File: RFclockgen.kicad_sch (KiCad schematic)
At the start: 10 parts, among them J1 Conn_01x04_Pin, J3 Conn_01x02_Pin, U2 ESP32-S3-WROOM-1, U3 AP2112K-3.3

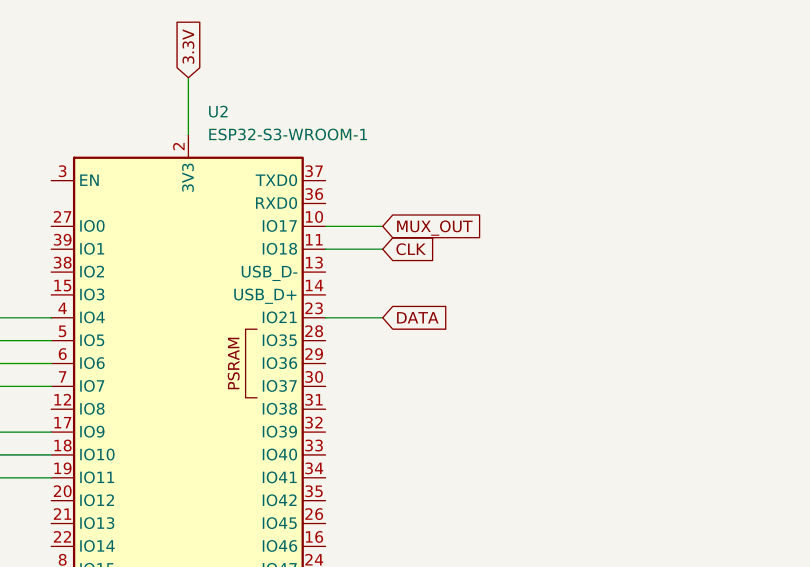
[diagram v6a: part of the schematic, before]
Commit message: Fix: fixed usb receptacle
Changed footprint and wired up usb C
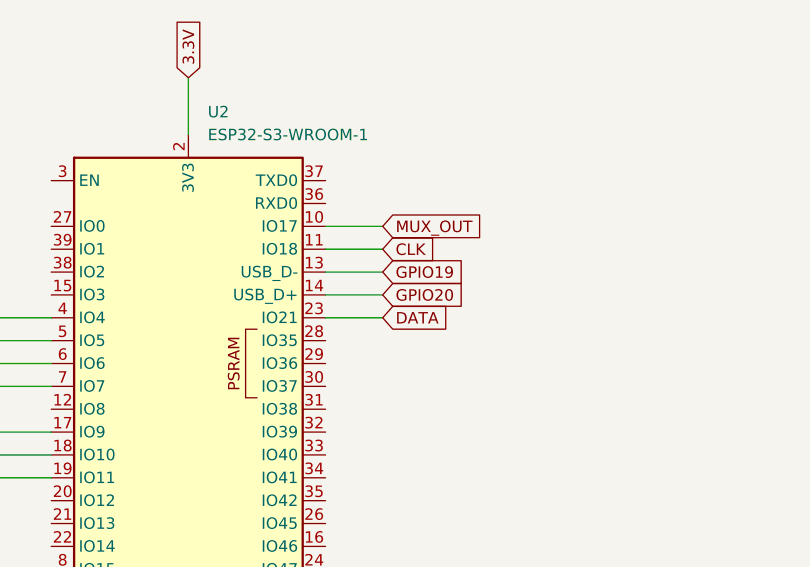
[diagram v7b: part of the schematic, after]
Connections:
- net GPIO19: now reaches U2.13 (USB_D-)
- net GPIO20: now reaches U2.14 (USB_D+)
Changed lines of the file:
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@@
+	(wire
+		(pts
+			(xy 172.72 68.58) (xy 179.07 68.58)
+		)
+		(stroke
+			(width 0)
+			(type default)
+		)
+	)
 	(wire
 		(pts
@@
 	(wire
 		(pts
+			(xy 172.72 66.04) (xy 179.07 66.04)
+		)
+		(stroke
+			(width 0)
+			(type default)
+		)
+	)
+	(wire
+		(pts
 			(xy 118.11 83.82) (xy 142.24 83.82)
 		)
@@
 		)
 	)
+	(global_label "GPIO19"
+		(shape input)
+		(at 179.07 66.04 0)
+		(fields_autoplaced yes)
+		(effects
+			(font
+				(size 1.27 1.27)
+			)
+			(justify left)
+		)
+		(property "Intersheetrefs" "${INTERSHEET_REFS}"
+			(at 188.9495 66.04 0)
+			(effects
+				(font
+					(size 1.27 1.27)
+				)
+				(justify left)
+				(hide yes)
+			)
+		)
+	)
 	(global_label "3.3V"
 		(shape input)
@@
 			(effects
 				(font
+					(size 1.27 1.27)
+				)
+				(justify left)
+				(hide yes)
+			)
+		)
+	)
+	(global_label "GPIO20"
+		(shape input)
+		(at 179.07 68.58 0)
+		(fields_autoplaced yes)
+		(effects
+			(font
+				(size 1.27 1.27)
+			)
+			(justify left)
+		)
+		(property "Intersheetrefs" "${INTERSHEET_REFS}"
+			(at 188.9495 68.58 0)
+			(effects
+				(font

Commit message: updated schematic
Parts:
- added C1, C4: 1u, symbol Device:C
- added U4: ESP32-C6-WROOM-1-N8, MOD28_ESP32-C6-WROOM-1_EXP, symbol 2026-10-07_01-33-30:ESP32-C6-WROOM-1-N8
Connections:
- net GND: now also C1.2, C4.2
- net at U3.1 (VIN): now also C1.1
- net at FB1.2, FB2.1, U3.5 (VOUT): now also C4.1
- net GPIO19: no longer names the net of U2.13 (USB_D-)
- net GPIO20: no longer names the net of U2.14 (USB_D+)
